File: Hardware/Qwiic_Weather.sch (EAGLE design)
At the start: 25 parts, among them J1 QWIIC, J2 QWIIC, J3 PTH, U1 BME280

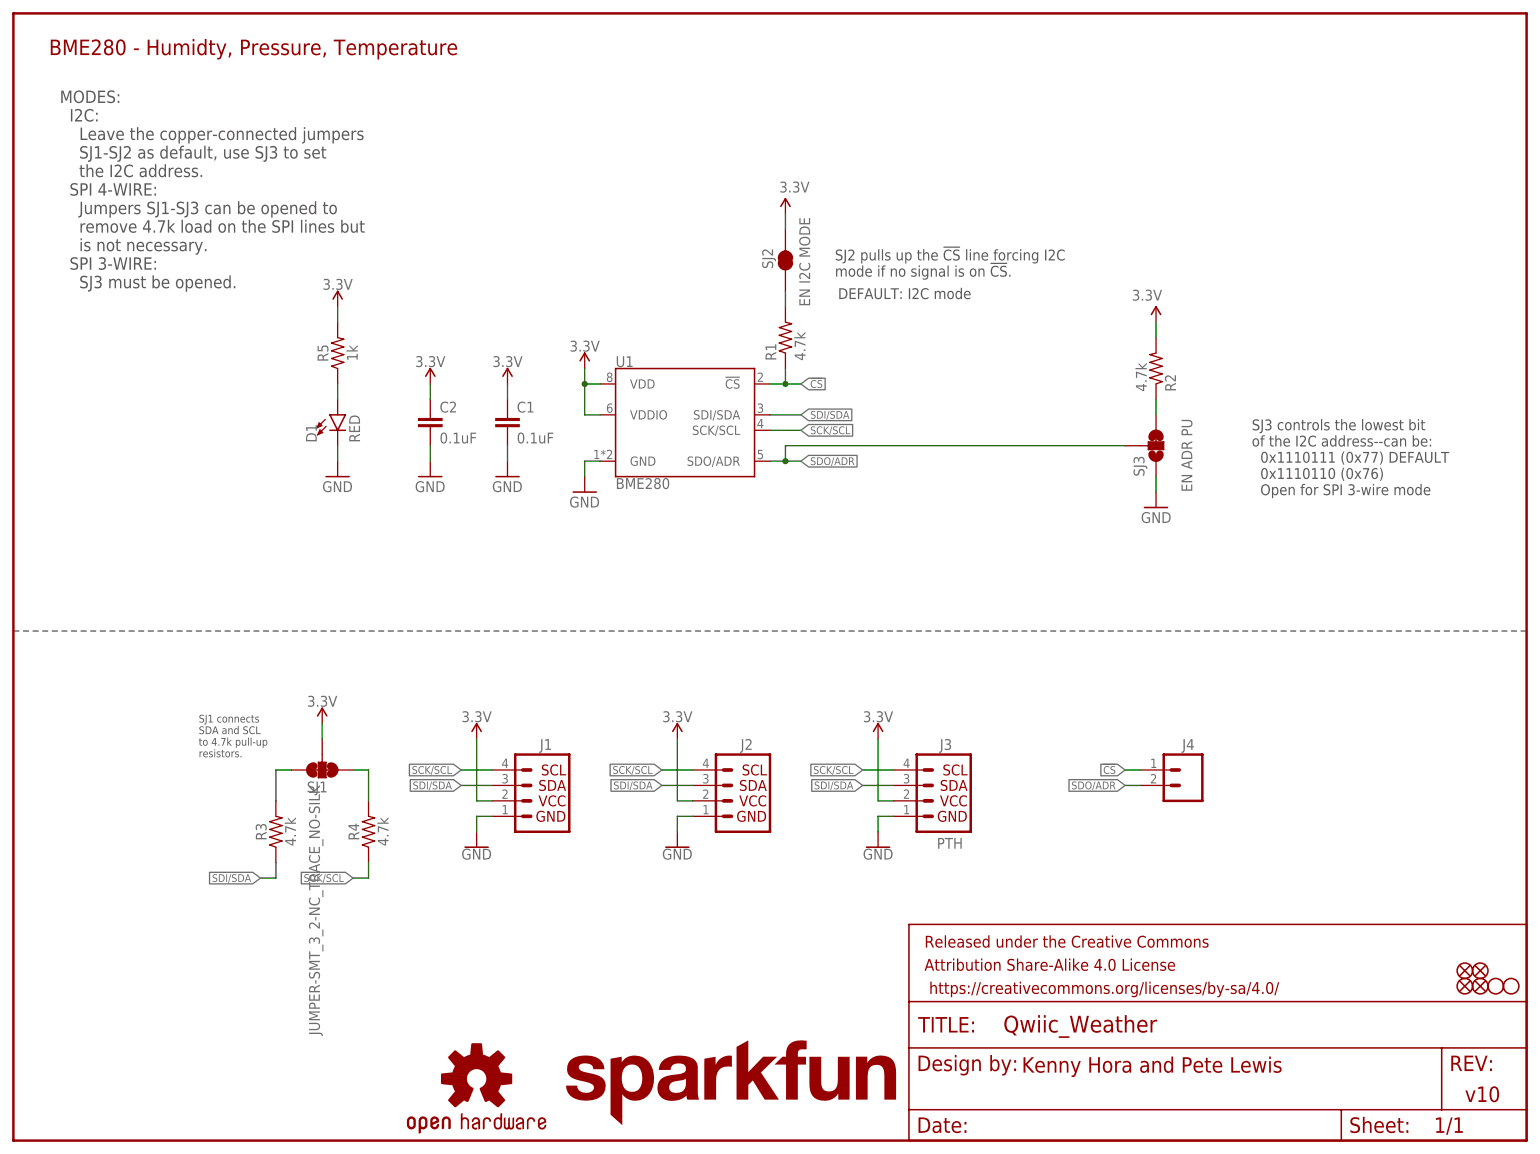
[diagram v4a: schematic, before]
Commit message: changes during checklist run 1
-moved all text in sch to vector
-removed unwanted value on jumper
-4pin pth connector replaced with sparkfun library
-vcc range added
-dimension width to 8 mils
-updated package on IC to fatten up silk width
-measures to inch
-Designer added to tdocu in brd
-nudged via to avoid silk on I2C label
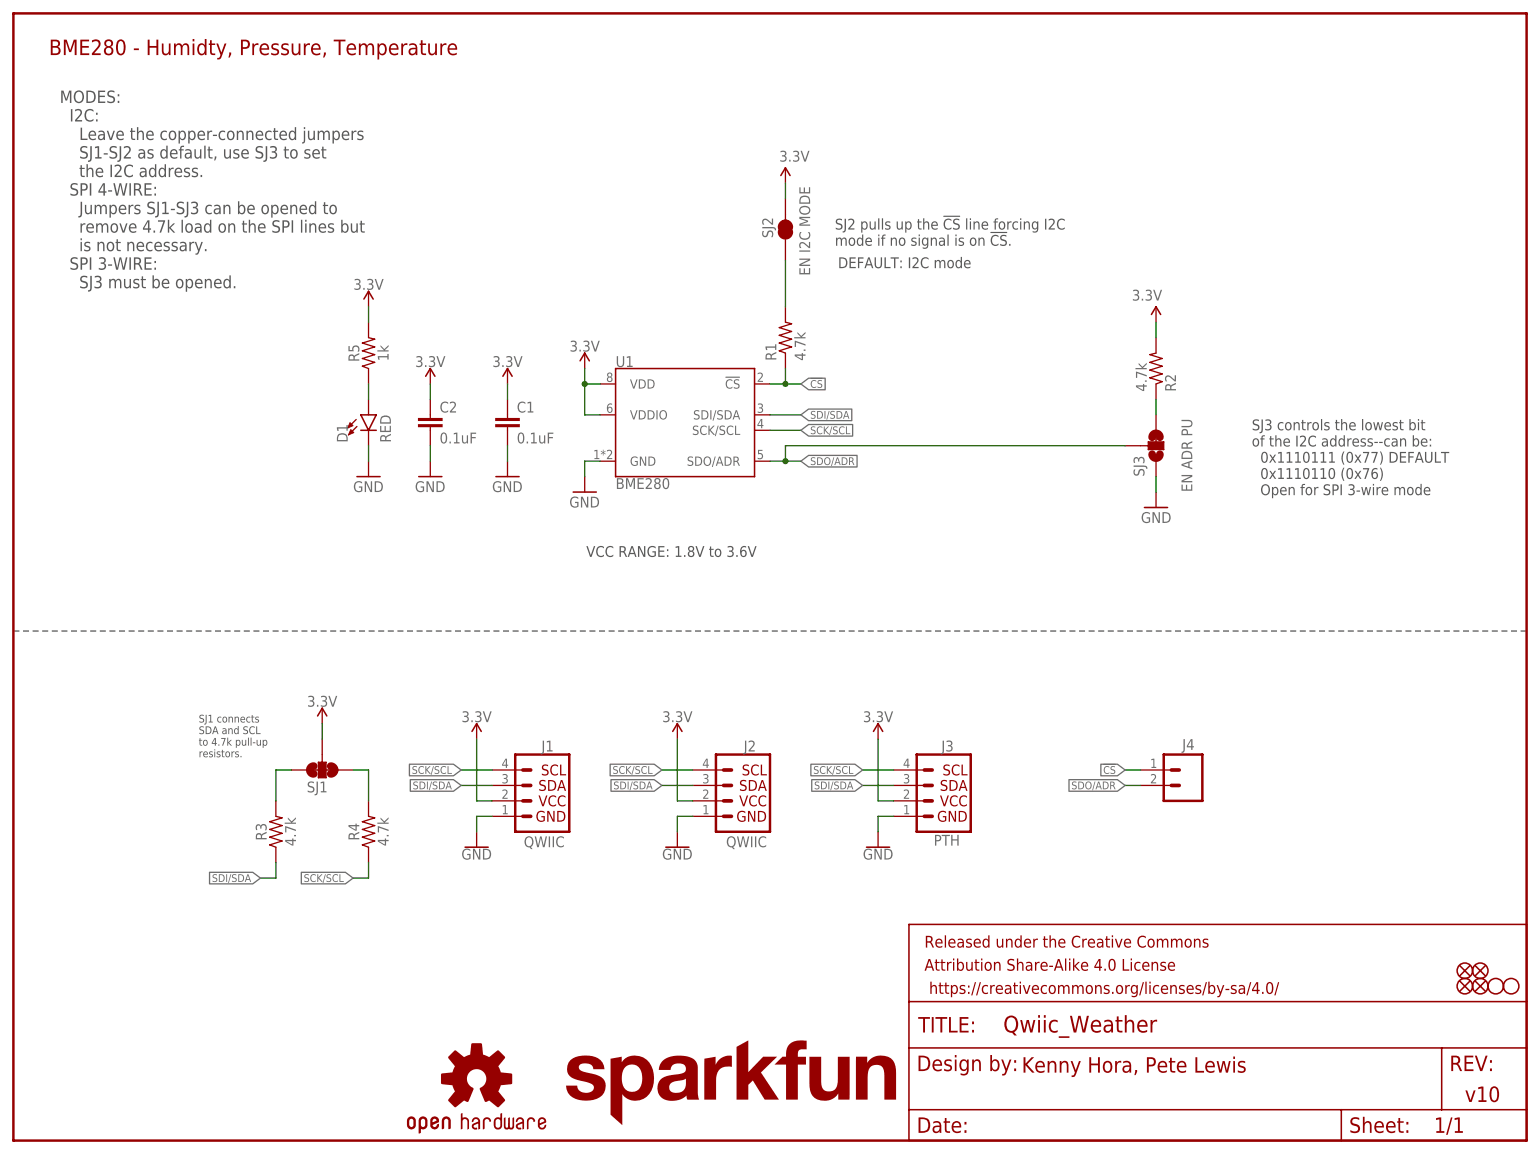
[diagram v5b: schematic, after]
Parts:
- J3: device SparkX:I2C_STANDARD_NO_SILK -> SparkFun-Connectors:I2C_STANDARD_NO_SILK
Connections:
- net 3.3V: now also J3.2; no longer J3.VCC
- net GND: now also J3.1; no longer J3.GND
- net SCK/SCL: now also J3.4; no longer J3.SCL
- net SDI/SDA: now also J3.3; no longer J3.SDA
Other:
- note added: "Kenny Hora, Pete Lewis"
- note added: "VCC RANGE: 1.8V to 3.6V"
- note removed: "Kenny Hora and Pete Lewis"
- moved on the sheet: D1, R5, SJ2

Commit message: Changes during/post group design review
-added power led disable jumper (and buzzard label and schematic text note).
-switched CS to "pointer" flag label cuz it's an input.
-added GND vias and nudges vias for better ground flow.
-changed info line to short dash.
-added text name for bottom half of schematic.
-moved fids added third standoff.
-Capitalized Temp Humidity Pressure text.
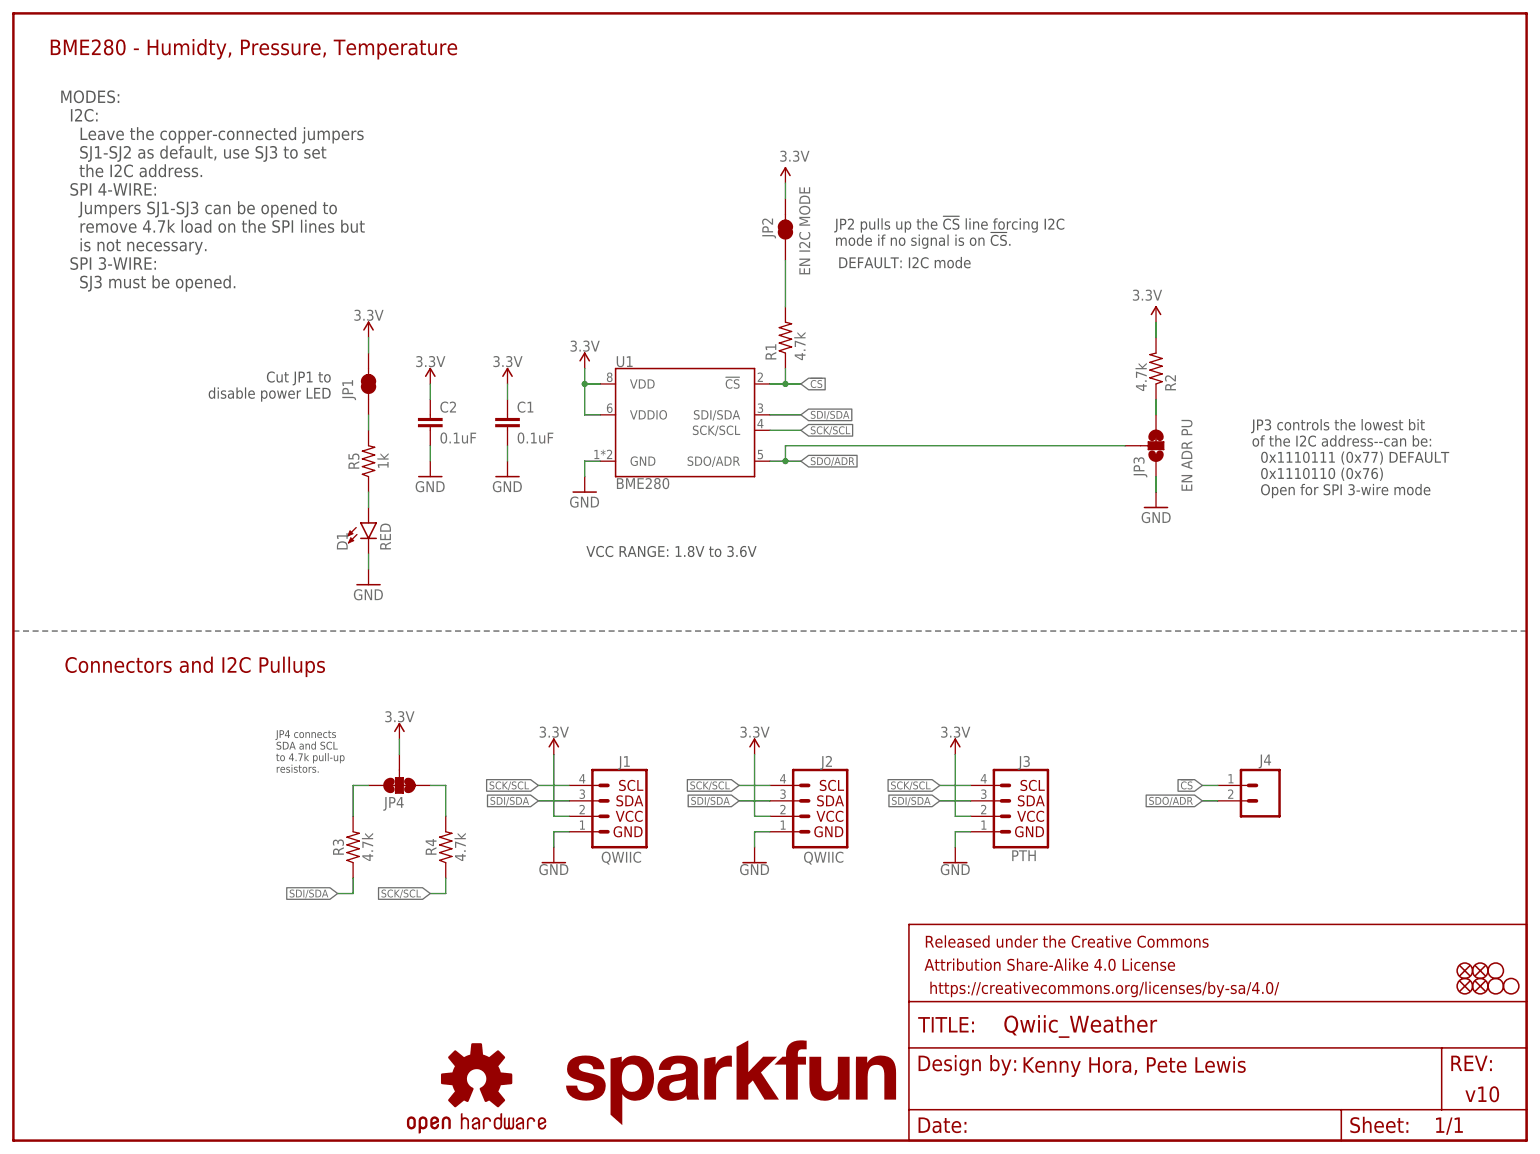
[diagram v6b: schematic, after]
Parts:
- removed SJ1: JUMPER-SMT_3_2-NC_TRACE_NO-SILK, SparkFun-Jumpers:JUMPER-SMT_3_2-NC_TRACE_NO-SILK
- added H1: STAND-OFF, SparkFun-Hardware:STAND-OFF
- added JP1: JUMPER-SMT_2_NC_TRACE_NO-SILK, SparkFun-Jumpers:JUMPER-SMT_2_NC_TRACE_NO-SILK
- added JP4: JUMPER-SMT_3_2-NC_TRACE_NO-SILK, SparkFun-Jumpers:JUMPER-SMT_3_2-NC_TRACE_NO-SILK
- renumbered SJ2 to JP2, SJ3 to JP3
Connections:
- new net N$7: JP1.1, R5.2
- net 3.3V: now also JP1.2, JP4.2; no longer R5.2, SJ1.2
- net N$4: now also JP4.3; no longer SJ1.3
- net N$5: now also JP4.1; no longer SJ1.1
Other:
- note added: "Connectors and I2C Pullups"
- note added: "Cut JP1 to disable power LED"
- note added: "JP2 pulls up the !CS! line forcing I2C mode if no signal is on !CS!."
- note added: "JP3 controls the lowest bit of the I2C address--can be: 0x1110111 (0x77) DEFAULT 0x1110110 (0x76) Open for SPI 3-wire mode"
- note added: "JP4 connects SDA and SCL to 4.7k pull-up resistors."
- note removed: "SJ1 connects SDA and SCL to 4.7k pull-up resistors."
- note removed: "SJ2 pulls up the !CS! line forcing I2C mode if no signal is on !CS!."
- note removed: "SJ3 controls the lowest bit of the I2C address--can be: 0x1110111 (0x77) DEFAULT 0x1110110 (0x76) Open for SPI 3-wire mode"
- moved on the sheet: D1, J1, J2, J3, J4, R3, R4, R5
